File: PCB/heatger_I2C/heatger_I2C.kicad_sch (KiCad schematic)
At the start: 21 parts, among them J2 Screen, J3 BME280, SW3 Next, SW4 Order, U1 P82B715DR, U2 PCF8574

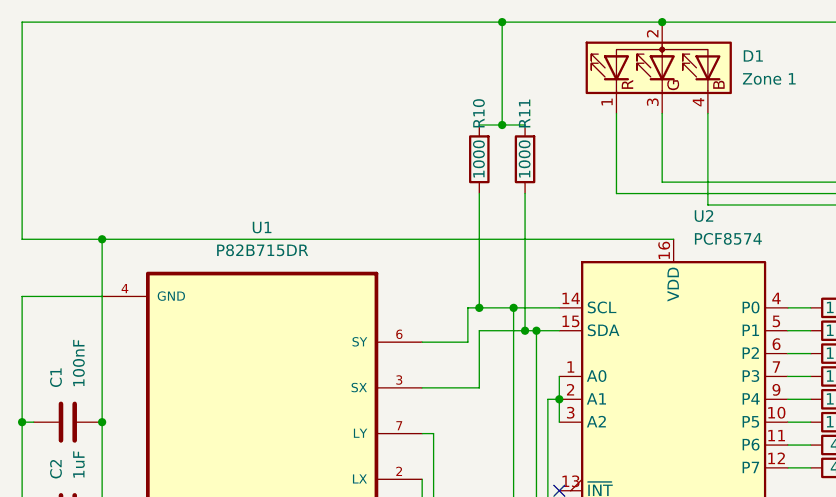
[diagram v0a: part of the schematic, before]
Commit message: add capacitors and gerbers files
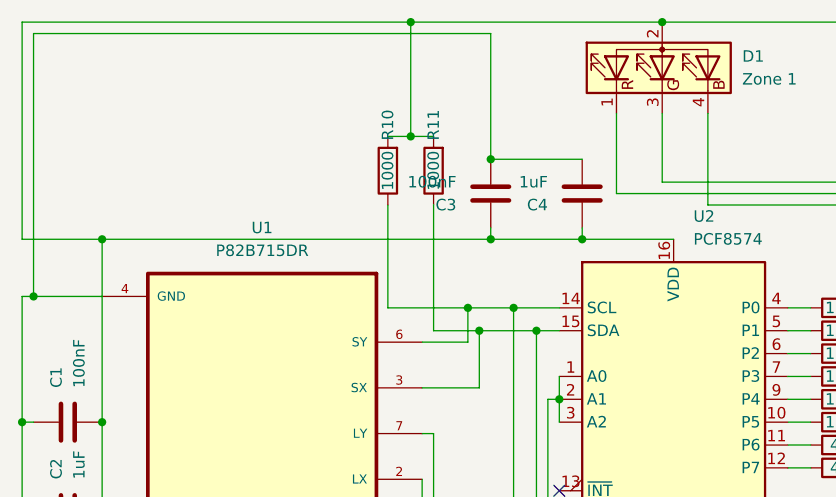
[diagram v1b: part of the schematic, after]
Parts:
- added C3: 100nF, Capacitor_SMD:C_0805_2012Metric_Pad1.18x1.45mm_HandSolder, symbol Device:C
- added C4: 1uF, Capacitor_SMD:C_0805_2012Metric_Pad1.18x1.45mm_HandSolder, symbol Device:C
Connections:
- net +5V: now also C3.1, C4.1
- net GND: now also C3.2, C4.2
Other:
- moved on the sheet: R10, R11

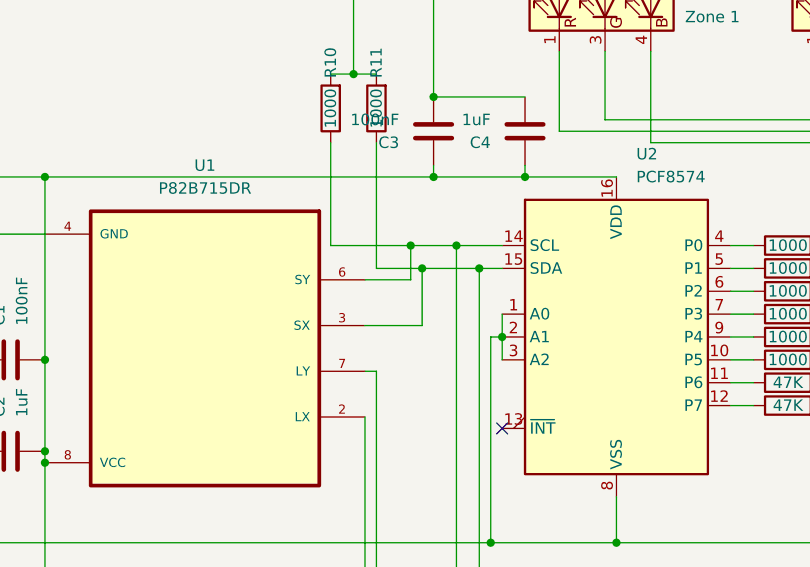
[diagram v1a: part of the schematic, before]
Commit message: invert wiring for pin headers
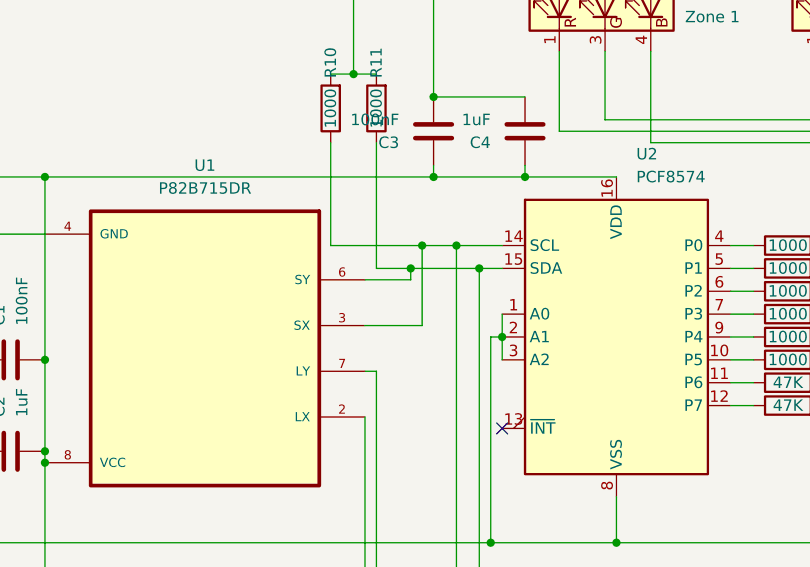
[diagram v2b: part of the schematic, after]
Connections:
- net at J2.2 (Pin_2), J3.3 (Pin_3), R10.1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: now also U1.3 (SX); no longer U1.6 (SY)
- net at J2.1 (Pin_1), J3.4 (Pin_4), R11.1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: now also U1.6 (SY); no longer U1.3 (SX)
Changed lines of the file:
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@@
   (junction (at 107.95 115.57) (diameter 0) (color 0 0 0 0)
   )
-  (junction (at 134.62 67.31) (diameter 0) (color 0 0 0 0)
-  )
   (junction (at 86.36 66.04) (diameter 0) (color 0 0 0 0)
   )
@@
   (junction (at 93.98 90.17) (diameter 0) (color 0 0 0 0)
   )
-  (junction (at 135.89 69.85) (diameter 0) (color 0 0 0 0)
+  (junction (at 134.62 69.85) (diameter 0) (color 0 0 0 0)
   )
   (junction (at 93.98 91.44) (diameter 0) (color 0 0 0 0)
@@
   )
   (junction (at 93.98 59.69) (diameter 0) (color 0 0 0 0)
+  )
+  (junction (at 135.89 67.31) (diameter 0) (color 0 0 0 0)
   )
   (no_connect (at 144.78 87.63))
@@
     (stroke (width 0) (type default))
   )
+  (wire (pts (xy 134.62 69.85) (xy 134.62 71.12))
+    (stroke (width 0) (type default))
+  )
   (wire (pts (xy 86.36 66.04) (xy 85.09 66.04))
     (stroke (width 0) (type default))
   )
-  (wire (pts (xy 135.89 69.85) (xy 135.89 76.2))
-    (stroke (width 0) (type default))
-  )
   (wire (pts (xy 189.23 74.93) (xy 196.85 74.93))
     (stroke (width 0) (type default))
@@
     (stroke (width 0) (type default))
   )
+  (wire (pts (xy 134.62 69.85) (xy 142.24 69.85))
+    (stroke (width 0) (type default))
+  )
   (wire (pts (xy 162.56 137.16) (xy 139.7 137.16))
     (stroke (width 0) (type default))
@@
     (stroke (width 0) (type default))
   )
-  (wire (pts (xy 130.81 69.85) (xy 135.89 69.85))
+  (wire (pts (xy 130.81 69.85) (xy 134.62 69.85))
     (stroke (width 0) (type default))
   )
@@
     (stroke (width 0) (type default))
   )
-  (wire (pts (xy 134.62 67.31) (xy 134.62 71.12))
-    (stroke (width 0) (type default))
-  )
   (wire (pts (xy 184.15 52.07) (xy 184.15 77.47))
     (stroke (width 0) (type default))
   )
-  (wire (pts (xy 134.62 67.31) (xy 139.7 67.31))
-    (stroke (width 0) (type default))
-  )
   (wire (pts (xy 137.16 59.69) (xy 93.98 59.69))
     (stroke (width 0) (type default))
@@
     (stroke (width 0) (type default))
   )
-  (wire (pts (xy 135.89 69.85) (xy 142.24 69.85))
-    (stroke (width 0) (type default))
-  )
   (wire (pts (xy 137.16 135.89) (xy 137.16 142.24))
     (stroke (width 0) (type default))
@@
     (stroke (width 0) (type default))
   )
-  (wire (pts (xy 125.73 67.31) (xy 134.62 67.31))
+  (wire (pts (xy 125.73 67.31) (xy 135.89 67.31))
     (stroke (width 0) (type default))
   )
@@
     (stroke (width 0) (type default))
   )
+  (wire (pts (xy 135.89 67.31) (xy 139.7 67.31))
+    (stroke (width 0) (type default))
+  )
+  (wire (pts (xy 135.89 67.31) (xy 135.89 76.2))
+    (stroke (width 0) (type default))
+  )
